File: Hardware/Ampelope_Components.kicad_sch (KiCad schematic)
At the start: 101 parts, among them J1 Conn_01x12_Male, J18 SWD_Header, J19 USB_B_Micro, J2 Conn_01x12_Male, J3 Conn_01x12_Male, J4 Conn_01x12_Male, J5 Eurorack_16_pin_power, Q1 MMBT3904, Q2 MMBT3904, Q3 MMBT3904, Q4 MMBT3904, Q5 MMBT3904, U1 STM32G431RB, U2 AS3364, U3 LM1117-3.3, U4 TL074, U5 TL074, U6 TL074, Y1 8MHz 20pF

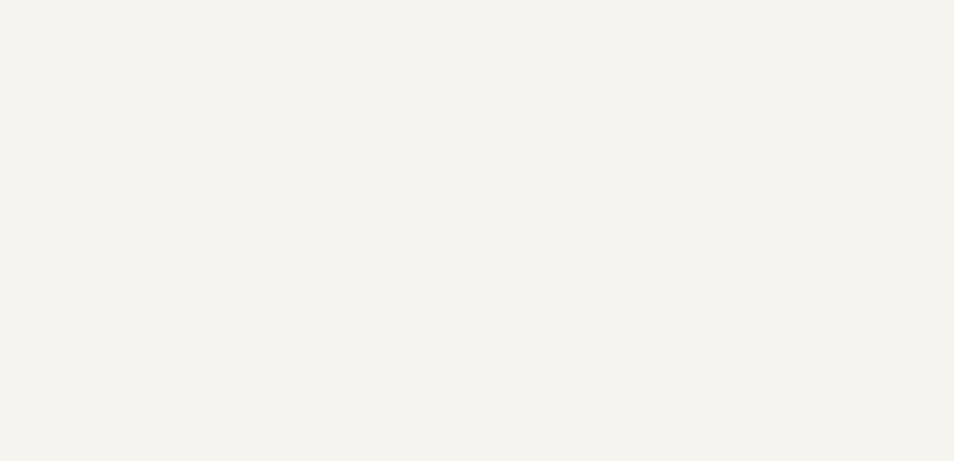
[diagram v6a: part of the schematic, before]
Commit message: Component layout refinement; pre change of input protection transistors to PNPs
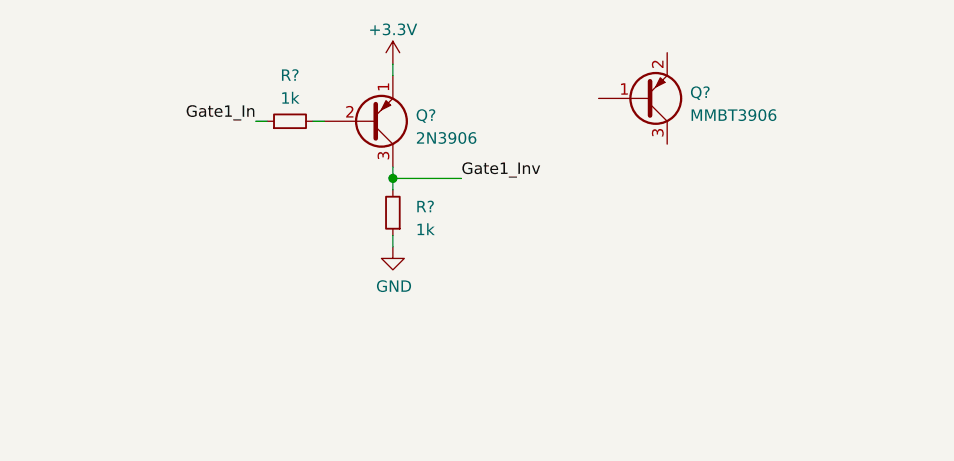
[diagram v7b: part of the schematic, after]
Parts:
- added Q?: MMBT3906, Package_TO_SOT_SMD:SOT-23, symbol Transistor_BJT:MMBT3906
- added Q?: 2N3906, Package_TO_SOT_THT:TO-92_Inline, symbol Transistor_BJT:2N3906
- added R? (x2): 1k, Resistor_SMD:R_0603_1608Metric_Pad0.98x0.95mm_HandSolder, symbol Device:R_Small
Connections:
- net +3V3: now also Q?.1 (E)
- net GND: now also R?.1
- net Gate1_In: now also R?.1
- net Gate1_Inv: now also Q?.3 (C), R?.2
- new net: Q?.2 (B), R?.2
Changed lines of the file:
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@@
   (junction (at 152.4 106.68) (diameter 1.016) (color 0 0 0 0))
   (junction (at 152.4 142.24) (diameter 1.016) (color 0 0 0 0))
+  (junction (at 153.67 -21.59) (diameter 1.016) (color 0 0 0 0))
   (junction (at 157.48 185.42) (diameter 1.016) (color 0 0 0 0))
   (junction (at 157.48 231.14) (diameter 1.016) (color 0 0 0 0))
@@
     (stroke (width 0) (type solid) (color 0 0 0 0))
   )
+  (wire (pts (xy 138.43 -27.94) (xy 139.7 -27.94))
+    (stroke (width 0) (type solid) (color 0 0 0 0))
+  )
   (wire (pts (xy 139.7 201.93) (xy 139.7 223.52))
     (stroke (width 0) (type solid) (color 0 0 0 0))
@@
     (stroke (width 0) (type solid) (color 0 0 0 0))
   )
+  (wire (pts (xy 144.78 -27.94) (xy 146.05 -27.94))
+    (stroke (width 0) (type solid) (color 0 0 0 0))
+  )
   (wire (pts (xy 144.78 224.79) (xy 144.78 229.87))
     (stroke (width 0) (type solid) (color 0 0 0 0))
@@
     (stroke (width 0) (type solid) (color 0 0 0 0))
   )
+  (wire (pts (xy 153.67 -34.29) (xy 153.67 -33.02))
+    (stroke (width 0) (type solid) (color 0 0 0 0))
+  )
+  (wire (pts (xy 153.67 -22.86) (xy 153.67 -21.59))
+    (stroke (width 0) (type solid) (color 0 0 0 0))
+  )
+  (wire (pts (xy 153.67 -21.59) (xy 153.67 -20.32))
+    (stroke (width 0) (type solid) (color 0 0 0 0))
+  )
+  (wire (pts (xy 153.67 -21.59) (xy 161.29 -21.59))
+    (stroke (width 0) (type solid) (color 0 0 0 0))
+  )
+  (wire (pts (xy 153.67 -15.24) (xy 153.67 -13.97))
+    (stroke (width 0) (type solid) (color 0 0 0 0))
+  )
   (wire (pts (xy 153.67 231.14) (xy 153.67 237.49))
     (stroke (width 0) (type solid) (color 0 0 0 0))
@@
     (effects (font (size 1.27 1.27)) (justify right bottom))
   )
+  (label "Gate1_In" (at 138.43 -27.94 180)
+    (effects (font (size 1.27 1.27)) (justify right bottom))
+  )
   (label "Gate1_Inv" (at 160.02 36.83 0)
     (effects (font (size 1.27 1.27)) (justify left bottom))
@@
     (effects (font (size 1.27 1.27)) (justify left bottom))
   )
+  (label "Gate1_Inv" (at 161.29 -21.59 0)
+    (effects (font (size 1.27 1.27)) (justify left bottom))
+  )
   (label "Audio1_VCA" (at 171.45 194.31 0)
     (effects (font (size 1.27 1.27)) (justify left bottom))
@@
     (pin "1")
   )
+  (symbol (lib_id "power:+3.3V") (at 153.67 -34.29 0) (unit 1)
+    (in_bom yes) (on_board yes)
+    (property "Reference" "#PWR?" (id 0) (at 153.67 -30.48 0)
+      (effects (font (size 1.27 1.27)) hide)
+    )
+    (property "Value" "+3.3V" (id 1) (at 153.67 -38.1 0))
+    (property "Footprint" "" (id 2) (at 153.67 -34.29 0)
+      (effects (font (size 1.27 1.27)) hide)
+    )
+    (property "Datasheet" "" (id 3) (at 153.67 -34.29 0)
+      (effects (font (size 1.27 1.27)) hide)
+    )
+    (pin "1")
+  )
   (symbol (lib_id "power:VCC") (at 157.48 182.88 0) (unit 1)
     (in_bom yes) (on_board yes)
@@
     (pin "1")
   )
+  (symbol (lib_id "power:GND") (at 153.67 -13.97 0) (unit 1)
+    (in_bom yes) (on_board yes)
+    (property "Reference" "#PWR?" (id 0) (at 153.67 -7.62 0)
+      (effects (font (size 1.27 1.27)) hide)
+    )
+    (property "Value" "GND" (id 1) (at 153.797 -9.5758 0))
+    (property "Footprint" "" (id 2) (at 153.67 -13.97 0)
+      (effects (font (size 1.27 1.27)) hide)
+    )
+    (property "Datasheet" "" (id 3) (at 153.67 -13.97 0)
+      (effects (font (size 1.27 1.27)) hide)
+    )
+    (pin "1")
+  )
   (symbol (lib_id "power:GND") (at 153.67 243.84 0) (unit 1)
     (in_bom yes) (on_board yes)
@@
     (pin "2")
   )
+  (symbol (lib_id "Device:R_Small") (at 142.24 -27.94 90) (unit 1)
+    (in_bom yes) (on_board yes) (fields_autoplaced)
+    (property "Reference" "R?" (id 0) (at 142.24 -33.02 90))
+    (property "Value" "1k" (id 1) (at 142.24 -30.48 90))
+    (property "Footprint" "Resistor_SMD:R_0603_1608Metric_Pad0.98x0.95mm_HandSolder" (id 2) (at 142.24 -27.94 0)
+      (effects (font (size 1.27 1.27)) hide)
+    )
+    (property "Datasheet" "~" (id 3) (at 142.24 -27.94 0)
+      (effects (font (size 1.27 1.27)) hide)
+    )
+    (pin "1")
+    (pin "2")
+  )
   (symbol (lib_id "Device:R_Small") (at 144.78 232.41 180) (unit 1)
     (in_bom yes) (on_board yes)
@@
     (pin "2")
   )
+  (symbol (lib_id "Device:R_Small") (at 153.67 -17.78 180) (unit 1)
+    (in_bom yes) (on_board yes) (fields_autoplaced)
+    (property "Reference" "R?" (id 0) (at 156.21 -18.4151 0)
+      (effects (font (size 1.27 1.27)) (justify right))
+    )
+    (property "Value" "1k" (id 1) (at 156.21 -15.8751 0)
+      (effects (font (size 1.27 1.27)) (justify right))
+    )
+    (property "Footprint" "Resistor_SMD:R_0603_1608Metric_Pad0.98x0.95mm_HandSolder" (id 2) (at 153.67 -17.78 0)
+      (effects (font (size 1.27 1.27)) hide)
+    )
+    (property "Datasheet" "~" (id 3) (at 153.67 -17.78 0)
+      (effects (font (size 1.27 1.27)) hide)
+    )
+    (pin "1")
+    (pin "2")
+  )
   (symbol (lib_id "Device:R_Small") (at 205.74 176.53 90) (unit 1)
     (in_bom yes) (on_board yes) (fields_autoplaced)
@@
     (pin "3")
   )
+  (symbol (lib_id "Transistor_BJT:2N3906") (at 151.13 -27.94 0) (mirror x) (unit 1)
+    (in_bom yes) (on_board yes) (fields_autoplaced)
+    (property "Reference" "Q?" (id 0) (at 156.21 -28.5751 0)
+      (effects (font (size 1.27 1.27)) (justify left))
+    )
+    (property "Value" "2N3906" (id 1) (at 156.21 -26.0351 0)
+      (effects (font (size 1.27 1.27)) (justify left))
+    )
+    (property "Footprint" "Package_TO_SOT_THT:TO-92_Inline" (id 2) (at 156.21 -29.845 0)
+      (effects (font (size 1.27 1.27) italic) (justify left) hide)
+    )
+    (property "Datasheet" "https://www.onsemi.com/pub/Collateral/2N3906-D.PDF" (id 3) (at 151.13 -27.94 0)
+      (effects (font (size 1.27 1.27)) (justify left) hide)
+    )
+    (pin "1")
+    (pin "2")
+    (pin "3")
+  )
+  (symbol (lib_id "Transistor_BJT:MMBT3906") (at 181.61 -30.48 0) (mirror x) (unit 1)
+    (in_bom yes) (on_board yes) (fields_autoplaced)
+    (property "Reference" "Q?" (id 0) (at 186.69 -31.1151 0)
+      (effects (font (size 1.27 1.27)) (justify left))
+    )
+    (property "Value" "MMBT3906" (id 1) (at 186.69 -28.5751 0)
+      (effects (font (size 1.27 1.27)) (justify left))
+    )
+    (property "Footprint" "Package_TO_SOT_SMD:SOT-23" (id 2) (at 186.69 -32.385 0)
+      (effects (font (size 1.27 1.27) italic) (justify left) hide)
+    )
+    (property "Datasheet" "https://www.onsemi.com/pub/Collateral/2N3906-D.PDF" (id 3) (at 181.61 -30.48 0)
+      (effects (font (size 1.27 1.27)) (justify left) hide)
+    )
+    (pin "1")
+    (pin "2")
+    (pin "3")
+  )
   (symbol (lib_id "Transistor_BJT:MMBT3904") (at 214.63 176.53 0) (unit 1)
     (in_bom yes) (on_board yes) (fields_autoplaced)
@@
       (reference "#PWR0102") (unit 1) (value "GND") (footprint "")
     )
+    (path "/2b8d2477-4af9-4fde-82d8-dc504dd62970"
+      (reference "#PWR?") (unit 1) (value "+3.3V") (footprint "")
+    )
+    (path "/6d98bc78-5004-49fc-95c4-52fdaa5892a2"
+      (reference "#PWR?") (unit 1) (value "GND") (footprint "")
+    )
     (path "/38b74e33-9547-4245-b81f-77c42914db02"
       (reference "C1") (unit 1) (value "1uF") (footprint "Capacitor_SMD:C_0603_1608Metric_Pad1.08x0.95mm_HandSolder")
@@
       (reference "Q5") (unit 1) (value "MMBT3904") (footprint "Package_TO_SOT_SMD:SOT-23")
     )
+    (path "/970ba9b5-eb4b-4bc1-bede-f40729b060f7"
+      (reference "Q?") (unit 1) (value "MMBT3906") (footprint "Package_TO_SOT_SMD:SOT-23")
+    )
+    (path "/b19bc84c-aded-4d82-a73d-cd072a7c5093"
+      (reference "Q?") (unit 1) (value "2N3906") (footprint "Package_TO_SOT_THT:TO-92_Inline")
+    )
     (path "/afdaa434-701d-4d23-a31e-7aa11c74bc7f"
       (reference "R1") (unit 1) (value "100k") (footprint "Resistor_SMD:R_0603_1608Metric_Pad0.98x0.95mm_HandSolder")
@@
       (reference "R52") (unit 1) (value "1k") (footprint "Resistor_SMD:R_0603_1608Metric_Pad0.98x0.95mm_HandSolder")
     )
+    (path "/50701a11-5c2d-4799-ba65-77989934f4ec"
+      (reference "R?") (unit 1) (value "1k") (footprint "Resistor_SMD:R_0603_1608Metric_Pad0.98x0.95mm_HandSolder")
+    )
+    (path "/b1e4c8f2-0318-4a60-9776-3b814a986e66"
+      (reference "R?") (unit 1) (value "1k") (footprint "Resistor_SMD:R_0603_1608Metric_Pad0.98x0.95mm_HandSolder")
+    )
     (path "/7615093a-318c-4c05-a9b3-abeff2838590"

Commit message: Updated to work correctly with AS3364 (gain levels, non inverting etc)
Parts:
- removed Q1, Q2, Q3, Q4, Q5: MMBT3904, Package_TO_SOT_SMD:SOT-23, symbol Transistor_BJT:MMBT3904
- removed Q?: MMBT3906, Package_TO_SOT_SMD:SOT-23, symbol Transistor_BJT:MMBT3906
- removed Q?: 2N3906, Package_TO_SOT_THT:TO-92_Inline, symbol Transistor_BJT:2N3906
- removed R35, R37, R39, R41: 75k, Resistor_SMD:R_0603_1608Metric_Pad0.98x0.95mm_HandSolder, symbol Device:R
- removed R? (x2): 1k, Resistor_SMD:R_0603_1608Metric_Pad0.98x0.95mm_HandSolder, symbol Device:R_Small
- added C? (x4): 2.2nF, Capacitor_SMD:C_0603_1608Metric_Pad1.08x0.95mm_HandSolder, symbol Device:C_Small
- added Q1, Q2, Q3, Q4, Q5: MMBT3906, Package_TO_SOT_SMD:SOT-23, symbol Transistor_BJT:MMBT3906
- added R? (x4): 6k8, Resistor_SMD:R_0603_1608Metric_Pad0.98x0.95mm_HandSolder, symbol Device:R_Small
- added R? (x4): 10k, Resistor_SMD:R_0603_1608Metric_Pad0.98x0.95mm_HandSolder, symbol Device:R_Small
- R36, R38, R40, R42: value 20k -> 3k3
- R43, R44, R45, R46: value 47k -> 4k7
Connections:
- net +3V3: now also Q1.2 (E), Q2.2 (E), Q3.2 (E), Q4.2 (E), Q5.2 (E); no longer R15.2, R16.2, R17.2, R18.2, R49.2
- net Audio2_In: now also J2.4 (Pin_4); no longer J2.3 (Pin_3)
- net Audio3_In: now also J2.5 (Pin_5); no longer J2.4 (Pin_4)
- net Clock_Inv: now also Q5.3 (C)
- net Env1_DAC: now also U6.3 (+), R?.1; no longer R36.2, U2.3 (VC1)
- net Env2_DAC: now also U6.5 (+), R?.1; no longer R38.2, U2.6 (VC2)
- net Env3_DAC: now also U6.10 (+), R?.1; no longer R40.2, U2.11 (VC3)
- net Env4_DAC: now also U6.12 (+), R?.1; no longer R42.2, U2.14 (VC4)
- net GND: now also R15.2, R16.2, R17.2, R18.2, R36.2, R38.2, R40.2, R42.2, R49.2, C?.1, C?.1, C?.1, C?.1, R?.2, R?.2, R?.2, R?.2; no longer U6.10 (+), U6.12 (+), U6.3 (+), U6.5 (+)
- net Gate1_Inv: now also Q1.3 (C)
- net Gate2_Inv: now also Q2.3 (C)
- net Gate3_Inv: now also Q3.3 (C)
- net Gate4_Inv: now also Q4.3 (C)
- net at R12.2: now also Q3.1 (B)
- net at R10.2: now also Q1.1 (B)
- net at R48.2: now also Q5.1 (B)
- net at R11.2: now also Q2.1 (B)
- net at R13.2: now also Q4.1 (B)
- net USB_VBUS: no longer names the net of J19.1 (VBUS)
- new net Env1_Scaled: C?.2, R?.1, R?.2, U2.3 (VC1)
- new net Env2_Scaled: C?.2, R?.1, R?.2, U2.6 (VC2)
- new net Env3_Scaled: C?.2, R?.1, R?.2, U2.11 (VC3)
- new net Env4_Scaled: C?.2, R?.1, R?.2, U2.14 (VC4)
- no-connect marks 6 -> 25
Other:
- note added: "6k8 and 10k converts 3.3V to 1.96V 2.2nF capacitor smooths sampling jumps"
- note added: "Full Scale: 8V"
- note added: "TODO: - Serial debug points - Power test points"
- note removed: "Full Scale: 7.7V"
- moved on the sheet: R10, R11, R12, R13, R15, R16, R17, R18, R36, R38, R40, R42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
